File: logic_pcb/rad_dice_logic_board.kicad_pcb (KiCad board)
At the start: 2 copper layers, 118 x 49 mm, 20 parts, among them J1 SAMPLE-GEIGER-CONNECTOR, J2 NIXIE-CONNECTOR-CS, J3 NIXIE-CONNECTOR-SCK-MOSI, J4 SWITCH-CONNECTOR, J5 POWER-5V, J6 GROUND, J7 TOGGLE-CONNECTOR, U1 ADAFRUIT-DS3231

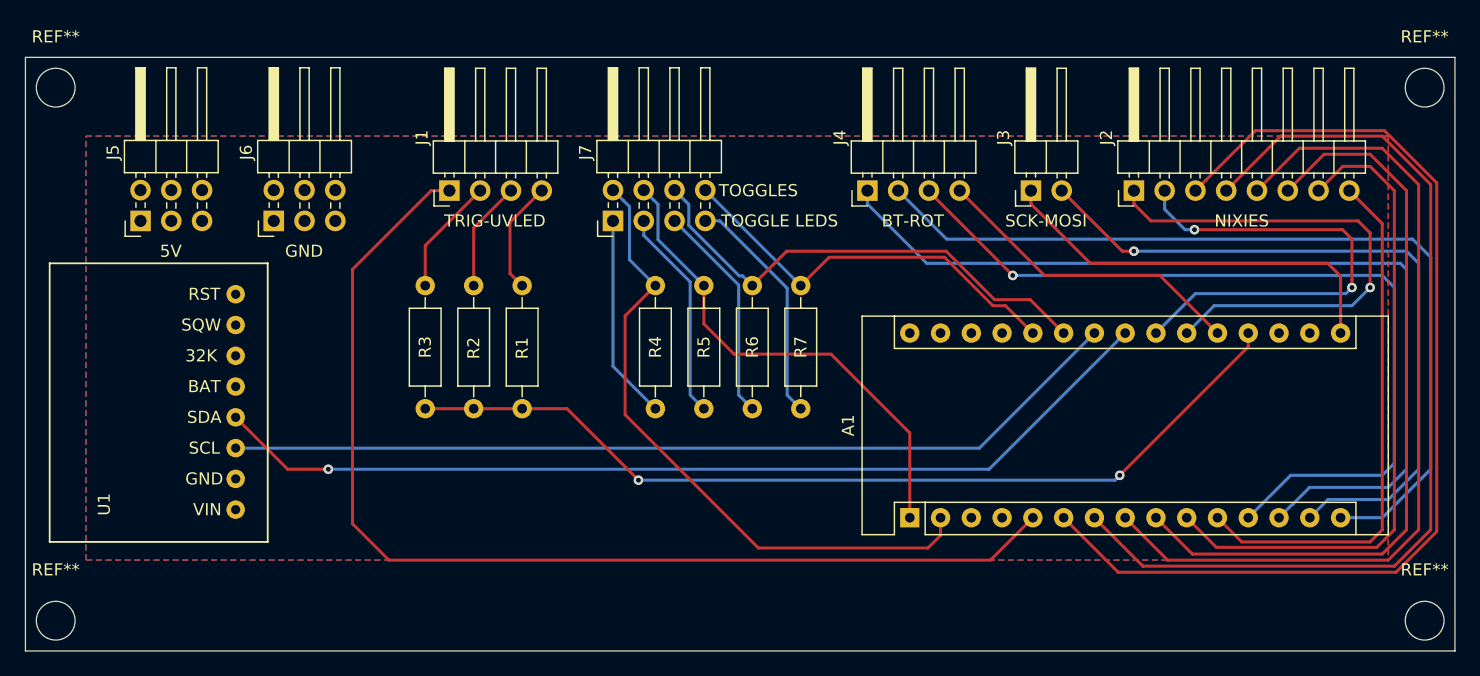
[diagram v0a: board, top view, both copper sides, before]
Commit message: update logic board for compatibility with front panel board
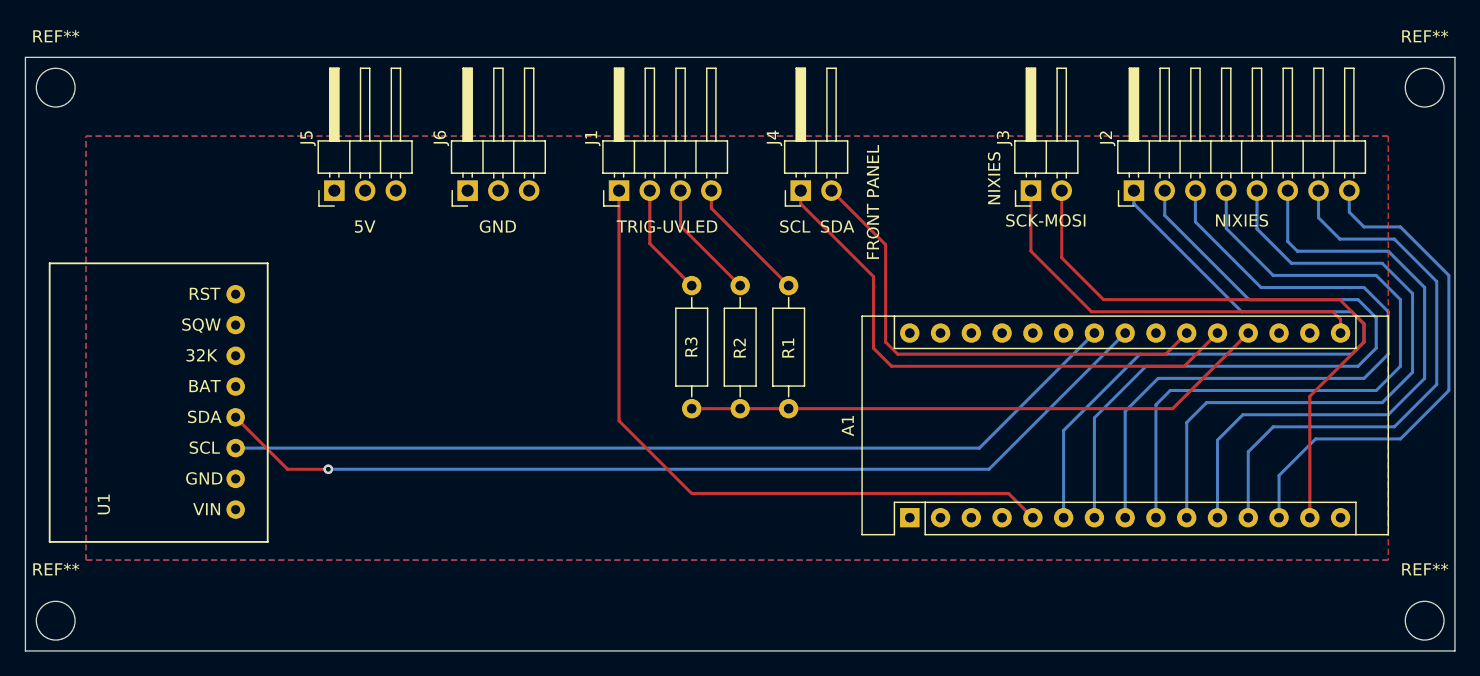
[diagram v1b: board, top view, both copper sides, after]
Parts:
- removed J7: TOGGLE-CONNECTOR, Pin_Headers:Pin_Header_Angled_2x04_Pitch2.54mm
- removed R4, R5, R6, R7: R, Resistors_THT:R_Axial_DIN0207_L6.3mm_D2.5mm_P10.16mm_Horizontal
- J4: value SWITCH-CONNECTOR -> FRONT-PANEL; footprint Pin_Headers:Pin_Header_Angled_1x04_Pitch2.54mm -> Pin_Headers:Pin_Header_Angled_1x02_Pitch2.54mm
- J5, J6: footprint Pin_Headers:Pin_Header_Angled_2x03_Pitch2.54mm -> Pin_Headers:Pin_Header_Angled_1x03_Pitch2.54mm
- moved R1 22.0 mm to (143.0, 100.0)
- moved R2 22.0 mm to (139.0, 100.0)
- moved R3 22.0 mm to (135.0, 100.0)
- moved J5 16.2 mm to (105.5, 82.0)
- moved J6 16.2 mm to (116.5, 82.0)
- moved J1 14.0 mm to (129.0, 82.0)
- moved J4 5.50 mm to (144.0, 82.0)
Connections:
- A1 pad 22: Net-(A1-Pad22) -> (no net)
- J2 pad 1: Net-(A1-Pad21) -> Net-(A1-Pad6)
- J2 pad 2: Net-(A1-Pad22) -> Net-(A1-Pad7)
- J2 pad 3: Net-(A1-Pad6) -> Net-(A1-Pad8)
- J2 pad 4: Net-(A1-Pad7) -> Net-(A1-Pad9)
- J2 pad 5: Net-(A1-Pad8) -> Net-(A1-Pad10)
- J2 pad 6: Net-(A1-Pad9) -> Net-(A1-Pad11)
- J2 pad 7: Net-(A1-Pad10) -> Net-(A1-Pad12)
- J2 pad 8: Net-(A1-Pad11) -> Net-(A1-Pad13)
- J4 pad 1: Net-(A1-Pad13) -> Net-(A1-Pad20)
- J4 pad 2: Net-(A1-Pad15) -> Net-(A1-Pad21)
- J5 pad 1: Net-(A1-Pad27) -> (no net)
- J5 pad 2: Net-(A1-Pad27) -> (no net)
- J5 pad 3: Net-(A1-Pad27) -> (no net)
- J6 pad 1: Net-(A1-Pad29) -> (no net)
- J6 pad 2: Net-(A1-Pad29) -> (no net)
- J6 pad 3: Net-(A1-Pad29) -> (no net)
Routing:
- net Net-(A1-Pad15): track 72.8 -> 0.00 mm
- net Net-(A1-Pad2): track 53.5 -> 0.00 mm
- net Net-(A1-Pad1): track 40.8 -> 0.00 mm
- net Net-(A1-Pad25): track 40.4 -> 0.00 mm
- net Net-(A1-Pad22): track 39.8 -> 0.00 mm, vias 2 -> 0
- net Net-(A1-Pad13): track 76.5 -> 42.1 mm
- net Net-(A1-Pad5): track 90.5 -> 56.5 mm
- net Net-(A1-Pad26): track 33.9 -> 0.00 mm
- net Net-(A1-Pad19): track 76.1 -> 48.5 mm, vias 2 -> 0
- net Net-(A1-Pad6): track 86.6 -> 60.7 mm
- net Net-(A1-Pad12): track 70.2 -> 46.0 mm, vias 1 -> 0
- net Net-(A1-Pad7): track 79.6 -> 59.4 mm
- net Net-(A1-Pad20): track 26.2 -> 45.6 mm
- net Net-(J7-Pad7): track 19.5 -> 0.00 mm
- net Net-(J7-Pad5): track 18.2 -> 0.00 mm
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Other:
- board text added: "FRONT PANEL"
- board text added: "GRIFFITH CYBERNETICS RAD DICE LOGIC BOARD REV. ALPHA-2 2019-09-07"
- board text added: "SCL"
- board text added: "SDA"
- board text removed: "BT-ROT"
- board text removed: "GRIFFITH CYBERNETICS RAD DICE LOGIC BOARD REV. ALPHA-1 2019-08-22"
- board text removed: "TOGGLE LEDS"
- board text removed: "TOGGLES"

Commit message: fix gnd/5v bug and add 2 gpio pins
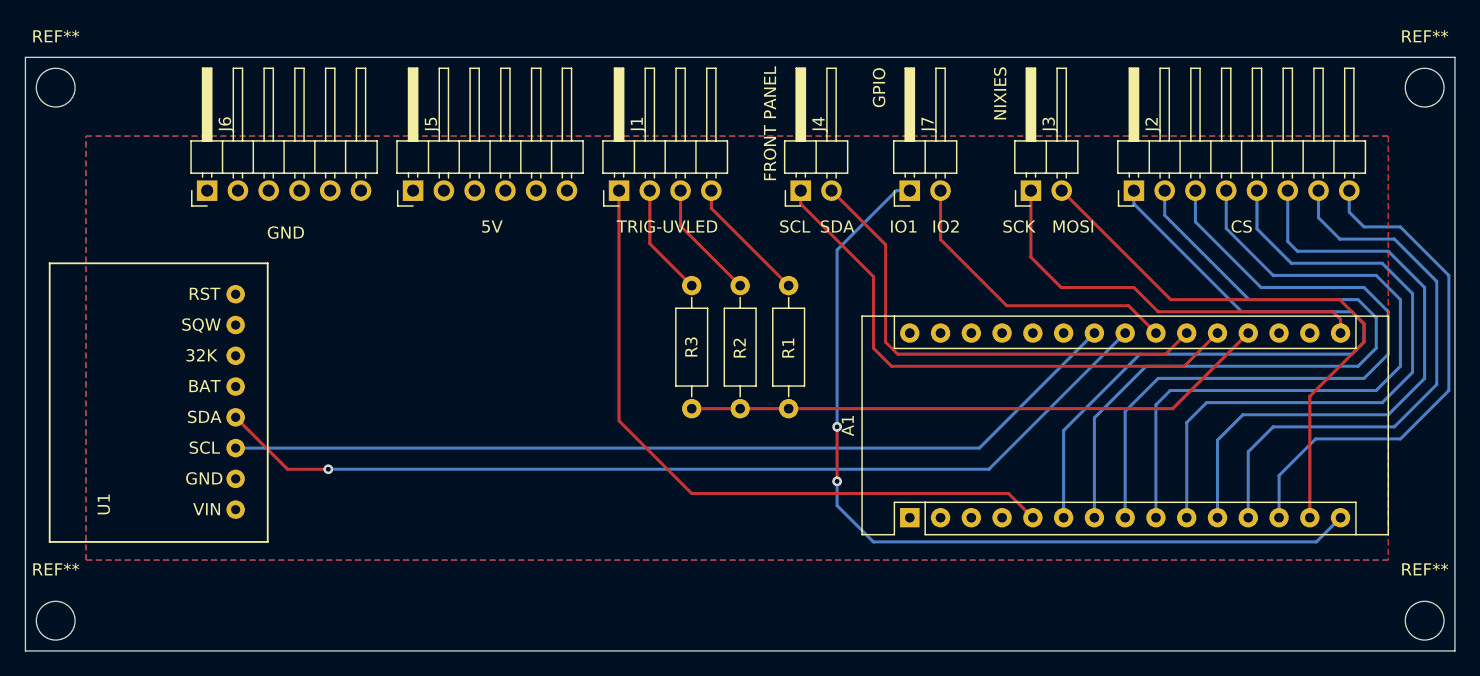
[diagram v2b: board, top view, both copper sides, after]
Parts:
- added J7: GPIO, Pin_Headers:Pin_Header_Angled_1x02_Pitch2.54mm, F.Cu at (153.0, 82.0)
- J5, J6: footprint Pin_Headers:Pin_Header_Angled_1x03_Pitch2.54mm -> Pin_Headers:Pin_Header_Angled_1x06_Pitch2.54mm
- moved J6 21.5 mm to (95.0, 82.0)
- moved J5 6.50 mm to (112.0, 82.0)
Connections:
- A1 pad 1: Net-(A1-Pad1) -> (no net)
- A1 pad 2: Net-(A1-Pad2) -> (no net)
- A1 pad 22: (no net) -> Net-(A1-Pad22)
- A1 pad 25: Net-(A1-Pad25) -> (no net)
- A1 pad 26: Net-(A1-Pad26) -> (no net)
- J5 pad 1: (no net) -> Net-(A1-Pad27)
- J5 pad 2: (no net) -> Net-(A1-Pad27)
- J5 pad 3: (no net) -> Net-(A1-Pad27)
- J6 pad 1: (no net) -> Net-(A1-Pad29)
- J6 pad 2: (no net) -> Net-(A1-Pad29)
- J6 pad 3: (no net) -> Net-(A1-Pad29)
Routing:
- net Net-(A1-Pad15): track 0.00 -> 72.8 mm, vias 0 -> 2
- net Net-(A1-Pad22): track 0.00 -> 25.0 mm
- net Net-(A1-Pad14): track 50.6 -> 47.4 mm
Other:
- board text added: "CHERNOBYL DICE LOGIC BOARD 2019-09-21"
- board text added: "CS"
- board text added: "GPIO"
- board text added: "IO1"
- board text added: "IO2"
- board text added: "MOSI"
- board text added: "SCK"
- board text removed: "GRIFFITH CYBERNETICS RAD DICE LOGIC BOARD REV. ALPHA-2 2019-09-07"
- board text removed: "SCK-MOSI"
